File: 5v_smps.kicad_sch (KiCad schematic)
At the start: 1 part

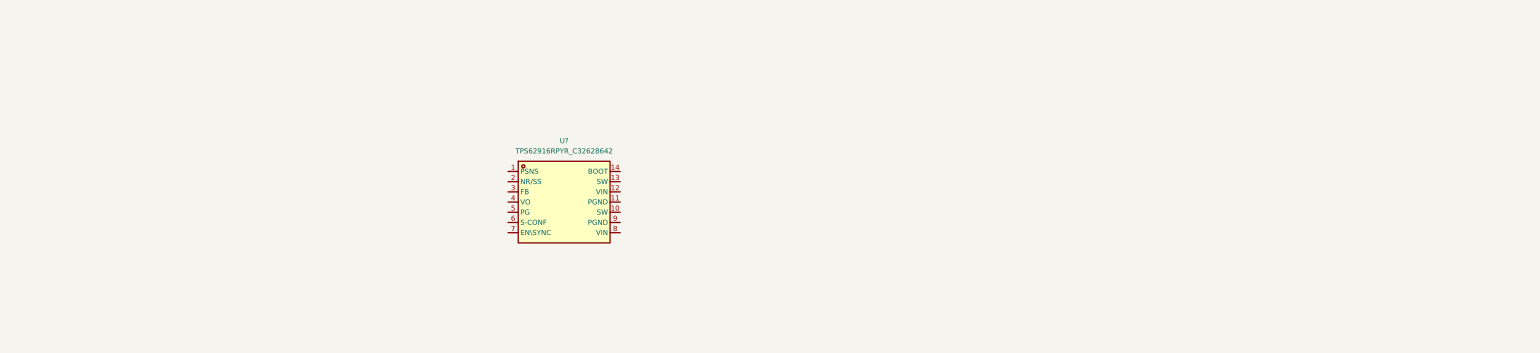
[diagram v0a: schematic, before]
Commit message: updated smps
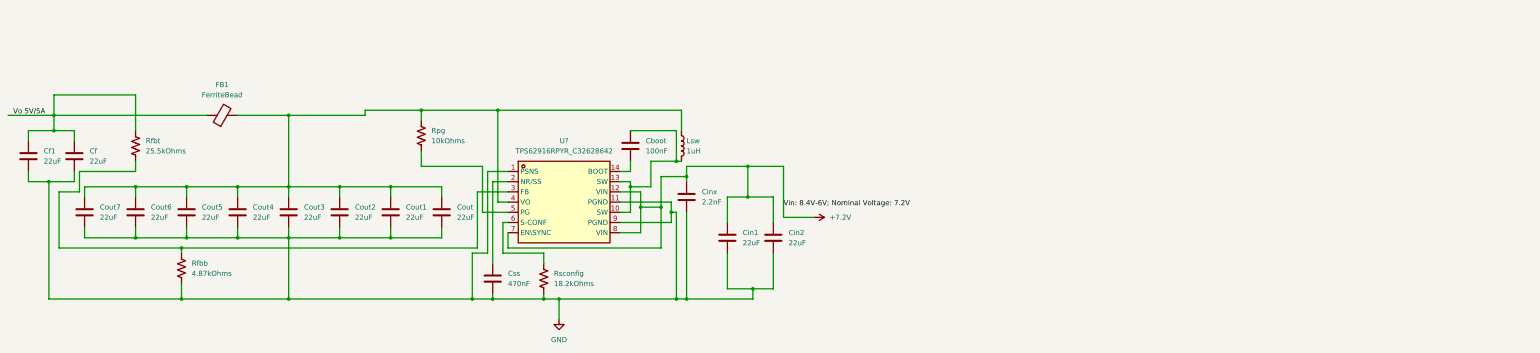
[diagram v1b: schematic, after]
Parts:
- added Cboot: 100nF, symbol Device:C
- added Cf, Cf1, Cin1, Cin2, Cout, Cout1, Cout2, Cout3, Cout4, Cout5, Cout6, Cout7: 22uF, symbol Device:C
- added Cinx: 2.2nF, symbol Device:C
- added Css: 470nF, symbol Device:C
- added FB1: FerriteBead, symbol Device:FerriteBead
- added Lsw: 1uH, symbol Device:L
- added Rfbb: 4.87kOhms, symbol 1_ECE_2300L_Components:Resistor
- added Rfbt: 25.5kOhms, symbol 1_ECE_2300L_Components:Resistor
- added Rpg: 10kOhms, symbol 1_ECE_2300L_Components:Resistor
- added Rsconfig: 18.2kOhms, symbol 1_ECE_2300L_Components:Resistor
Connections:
- net GND: now reaches U?.1 (PSNS)
- net GND: now also U?.11 (PGND), U?.9 (PGND), Cf.2, Cf1.2, Cin1.2, Cin2.2, Cinx.2, Cout.2, Cout1.2, Cout2.2, Cout3.2, Cout4.2, Cout5.2, Cout6.2, Cout7.2, Css.2, Rfbb.2, Rsconfig.2
- net at U?.10 (SW): now also U?.13 (SW), Cboot.1, Lsw.2
- net +7.2V: now reaches U?.12 (VIN)
- net +7.2V: now also U?.7 (EN\SYNC), U?.8 (VIN), Cin1.1, Cin2.1, Cinx.1
- net at U?.14 (BOOT): now also Cboot.2
- net at U?.2 (NR/SS): now also Css.1
- net at U?.3 (FB): now also Rfbb.1, Rfbt.2
- net at U?.4 (VO): now also Cout.1, Cout1.1, Cout2.1, Cout3.1, Cout4.1, Cout5.1, Cout6.1, Cout7.1, FB1.2, Lsw.1, Rpg.1
- net at U?.5 (PG): now also Rpg.2
- net at U?.6 (S-CONF): now also Rsconfig.1
- new net Vo 5V/5A: Cf.1, Cf1.1, FB1.1, Rfbt.1

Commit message: Clean up SMPS schematic
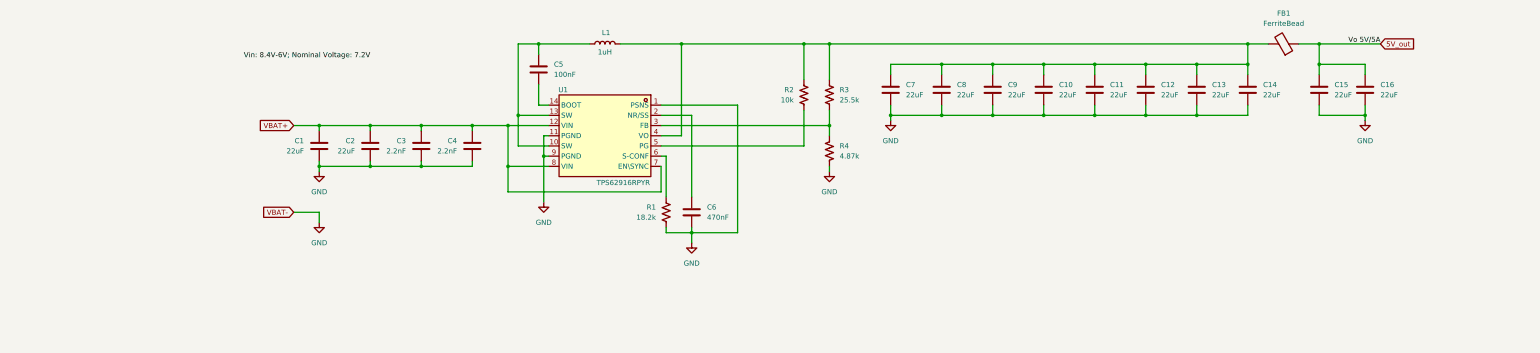
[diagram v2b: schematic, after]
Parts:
- removed Cout1, Cout2, Cout3, Cout4, Cout5, Cout6, Cout7: 22uF, symbol Device:C
- added C10, C11, C12, C13, C14, C8, C9: 22uF, symbol Device:C
- added C4: 2.2nF, Capacitor_SMD:C_0402_1005Metric, symbol Device:C
- C1: renamed from Cin2; footprint (none) -> Capacitor_SMD:C_1210_3225Metric
- C2: renamed from Cin1; footprint (none) -> Capacitor_SMD:C_1210_3225Metric
- C3: renamed from Cinx; footprint (none) -> Capacitor_SMD:C_0402_1005Metric
- R1: renamed from Rsconfig; value 18.2kOhms -> 18.2k
- R2: renamed from Rpg; value 10kOhms -> 10k
- R3: renamed from Rfbt; value 25.5kOhms -> 25.5k
- R4: renamed from Rfbb; value 4.87kOhms -> 4.87k
- U1: renamed from U?; value TPS62916RPYR_C32628642 -> TPS62916RPYR
- renumbered Cf to C15, Cf1 to C16, Cboot to C5, Css to C6, Cout to C7, Lsw to L1
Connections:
- net GND: now also C10.2, C11.2, C12.2, C13.2, C14.2, C4.2, C8.2, C9.2
- net at C7.1, FB1.2, L1.1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: now also R3.1, C10.1, C11.1, C12.1, C13.1, C14.1, C8.1, C9.1
- net +7.2V renamed VBAT+
- net VBAT+: now also C4.1
- net Vo 5V/5A renamed 5V_out
- net 5V_out: no longer R3.1
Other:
- moved on the sheet: C1, C15, C16, C2, C3, C5, C6, C7, FB1, L1, R1, R2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

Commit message: Update 5v_smps.kicad_sch
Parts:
- C10, C11, C12, C13, C14, C15, C16, C5, C7, C8, C9: footprint (none) -> Capacitor_SMD:C_1206_3216Metric
- C3, C4: footprint Capacitor_SMD:C_0402_1005Metric -> Capacitor_SMD:C_0603_1608Metric
- Ce: renamed from C6; footprint (none) -> Capacitor_SMD:C_0603_1608Metric
- FB1: footprint (none) -> 1210
- L1: footprint (none) -> Inductor_SMD:L_Coilcraft_XAL5030-XXX
- R1, R2, R3, R4: footprint (none) -> Resistor_SMD:R_0402_1005Metric
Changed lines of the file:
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@@
 	)
 	(junction
-		(at 271.78 64.77)
+		(at 278.13 59.69)
 		(diameter 0)
 		(color 0 0 0 0)
 	)
 	(junction
-		(at 259.08 77.47)
+		(at 271.78 64.77)
 		(diameter 0)
 		(color 0 0 0 0)
 	)
 	(junction
-		(at 146.05 59.69)
+		(at 259.08 77.47)
 		(diameter 0)
 		(color 0 0 0 0)
 	)
 	(junction
-		(at 322.58 64.77)
+		(at 146.05 59.69)
 		(diameter 0)
 		(color 0 0 0 0)
@@
 	)
 	(junction
-		(at 284.48 77.47)
+		(at 278.13 64.77)
 		(diameter 0)
 		(color 0 0 0 0)
 	)
 	(junction
-		(at 322.58 59.69)
+		(at 284.48 77.47)
 		(diameter 0)
 		(color 0 0 0 0)
@@
 	(wire
 		(pts
-			(xy 322.58 59.69) (xy 322.58 64.77)
+			(xy 176.53 74.93) (xy 195.58 74.93)
 		)
 		(stroke
@@
 	(wire
 		(pts
-			(xy 176.53 74.93) (xy 195.58 74.93)
+			(xy 284.48 67.31) (xy 284.48 64.77)
 		)
 		(stroke
@@
 	(wire
 		(pts
-			(xy 284.48 67.31) (xy 284.48 64.77)
+			(xy 184.15 105.41) (xy 184.15 106.68)
 		)
 		(stroke
@@
 	(wire
 		(pts
-			(xy 184.15 105.41) (xy 184.15 106.68)
+			(xy 278.13 64.77) (xy 284.48 64.77)
 		)
 		(stroke
@@
 	(wire
 		(pts
-			(xy 218.44 59.69) (xy 322.58 59.69)
+			(xy 218.44 59.69) (xy 278.13 59.69)
 		)
 		(stroke
@@
 	(wire
 		(pts
-			(xy 322.58 64.77) (xy 309.88 64.77)
-		)
-		(stroke
-			(width 0)
-			(type default)
-		)
-	)
-	(wire
-		(pts
 			(xy 271.78 77.47) (xy 259.08 77.47)
 		)
@@
 	(wire
 		(pts
+			(xy 233.68 64.77) (xy 233.68 67.31)
+		)
+		(stroke
+			(width 0)
+			(type default)
+		)
+	)
+	(wire
+		(pts
+			(xy 246.38 64.77) (xy 233.68 64.77)
+		)
+		(stroke
+			(width 0)
+			(type default)
+		)
+	)
+	(wire
+		(pts
 			(xy 129.54 80.01) (xy 138.43 80.01)
 		)
@@
 	(wire
 		(pts
+			(xy 278.13 59.69) (xy 278.13 64.77)
+		)
+		(stroke
+			(width 0)
+			(type default)
+		)
+	)
+	(wire
+		(pts
 			(xy 138.43 80.01) (xy 138.43 90.17)
 		)
@@
 	(wire
 		(pts
-			(xy 184.15 106.68) (xy 195.58 106.68)
+			(xy 246.38 64.77) (xy 259.08 64.77)
 		)
 		(stroke
@@
 	(wire
 		(pts
-			(xy 176.53 96.52) (xy 138.43 96.52)
+			(xy 184.15 106.68) (xy 195.58 106.68)
 		)
 		(stroke
@@
 	(wire
 		(pts
-			(xy 233.68 64.77) (xy 246.38 64.77)
+			(xy 176.53 96.52) (xy 138.43 96.52)
 		)
 		(stroke
@@
 	(wire
 		(pts
-			(xy 271.78 64.77) (xy 259.08 64.77)
+			(xy 176.53 82.55) (xy 181.61 82.55)
 		)
 		(stroke
@@
 	(wire
 		(pts
-			(xy 176.53 82.55) (xy 181.61 82.55)
+			(xy 271.78 64.77) (xy 259.08 64.77)
 		)
 		(stroke
@@
 	(wire
 		(pts
-			(xy 284.48 64.77) (xy 271.78 64.77)
+			(xy 309.88 64.77) (xy 297.18 64.77)
 		)
 		(stroke
@@
 	(wire
 		(pts
-			(xy 309.88 64.77) (xy 297.18 64.77)
+			(xy 176.53 85.09) (xy 212.09 85.09)
 		)
 		(stroke
@@
 	(wire
 		(pts
-			(xy 176.53 85.09) (xy 212.09 85.09)
+			(xy 309.88 64.77) (xy 322.58 64.77)
 		)
 		(stroke
@@
 	(wire
 		(pts
-			(xy 177.8 87.63) (xy 177.8 97.79)
+			(xy 284.48 64.77) (xy 297.18 64.77)
 		)
 		(stroke
@@
 	(wire
 		(pts
-			(xy 233.68 67.31) (xy 233.68 64.77)
+			(xy 177.8 87.63) (xy 177.8 97.79)
 		)
 		(stroke
@@
 	(wire
 		(pts
-			(xy 166.37 59.69) (xy 181.61 59.69)
+			(xy 278.13 59.69) (xy 327.66 59.69)
 		)
 		(stroke
@@
 	(wire
 		(pts
-			(xy 271.78 77.47) (xy 271.78 74.93)
+			(xy 166.37 59.69) (xy 181.61 59.69)
 		)
 		(stroke
@@
 	(wire
 		(pts
-			(xy 259.08 64.77) (xy 246.38 64.77)
+			(xy 271.78 77.47) (xy 271.78 74.93)
 		)
 		(stroke
@@
 	(wire
 		(pts
-			(xy 148.59 82.55) (xy 147.32 82.55)
+			(xy 278.13 64.77) (xy 271.78 64.77)
 		)
 		(stroke
@@
 	(wire
 		(pts
-			(xy 322.58 59.69) (xy 327.66 59.69)
+			(xy 148.59 82.55) (xy 147.32 82.55)
 		)
 		(stroke
@@
 	(wire
 		(pts
-			(xy 297.18 64.77) (xy 284.48 64.77)
-		)
-		(stroke
-			(width 0)
-			(type default)
-		)
-	)
-	(wire
-		(pts
 			(xy 116.84 90.17) (xy 129.54 90.17)
 		)
@@
 	)
 	(label "Vin: 8.4V-6V; Nominal Voltage: 7.2V"
-		(at 104.14 63.5 180)
+		(at 86.36 76.2 180)
 		(effects
 			(font
@@
 			)
 		)
-		(property "Footprint" ""
+		(property "Footprint" "Resistor_SMD:R_0402_1005Metric"
 			(at 178.816 101.854 90)
 			(effects
@@
 			)
 		)
-		(property "Footprint" "Capacitor_SMD:C_0402_1005Metric"
+		(property "Footprint" "Capacitor_SMD:C_0603_1608Metric"
 			(at 128.5748 88.9 0)
 			(effects
@@
 			)
 		)
-		(property "Footprint" ""
+		(property "Footprint" "Resistor_SMD:R_0402_1005Metric"
 			(at 219.456 72.644 90)
 			(effects
@@
 			)
 		)
-		(property "Footprint" ""
+		(property "Footprint" "Capacitor_SMD:C_1206_3216Metric"
 			(at 308.9148 74.93 0)
 			(effects
@@
 		(dnp no)
 		(fields_autoplaced yes)
-		(property "Reference" "C6"
+		(property "Reference" "Ce"
 			(at 187.96 100.3299 0)
 			(effects
@@
 			)
 		)
-		(property "Footprint" ""
+		(property "Footprint" "Capacitor_SMD:C_0603_1608Metric"
 			(at 183.1848 105.41 0)
 			(effects
@@
 			(project "ANTS-Power-board"
 				(path "/4d632659-7d2f-4407-ada5-b4e72f7be845/fb60ecbe-8c4e-46ea-aae5-ba0f80fe91e4"
-					(reference "C6")
+					(reference "Ce")
 					(unit 1)
 				)
@@
 			)
 		)
-		(property "Footprint" ""
+		(property "Footprint" "1210"
 			(at 331.47 61.468 90)
 			(effects
@@
 			)
 		)
-		(property "Footprint" ""
+		(property "Footprint" "Resistor_SMD:R_0402_1005Metric"
 			(at 217.424 86.614 90)
 			(effects
@@
 			)
 		)
-		(property "Footprint" ""
+		(property "Footprint" "Capacitor_SMD:C_1206_3216Metric"
 			(at 145.0848 69.85 0)
 			(effects
@@
 			)
 		)
-		(property "Footprint" ""
+		(property "Footprint" "Capacitor_SMD:C_1206_3216Metric"
 			(at 245.4148 74.93 0)
 			(effects
@@
 			)
 		)
-		(property "Footprint" ""
+		(property "Footprint" "Resistor_SMD:R_0402_1005Metric"
 			(at 213.106 72.644 90)
 			(effects
@@
 			)
 		)
-		(property "Footprint" ""
+		(property "Footprint" "Inductor_SMD:L_Coilcraft_XAL5030-XXX"
 			(at 162.56 59.69 0)
 			(effects
@@
 			)
 		)
-		(property "Footprint" ""
+		(property "Footprint" "Capacitor_SMD:C_1206_3216Metric"
 			(at 321.6148 74.93 0)
 			(effects
@@
 			)
 		)
-		(property "Footprint" ""
+		(property "Footprint" "Capacitor_SMD:C_1206_3216Metric"
 			(at 258.1148 74.93 0)
 			(effects
@@
 			)
 		)
-		(property "Footprint" ""
+		(property "Footprint" "Capacitor_SMD:C_1206_3216Metric"
 			(at 270.8148 74.93 0)
 			(effects
@@
 			)
 		)
-		(property "Footprint" "Capacitor_SMD:C_0402_1005Metric"
+		(property "Footprint" "Capacitor_SMD:C_0603_1608Metric"
 			(at 115.8748 88.9 0)
 			(effects
@@
 			)
 		)
-		(property "Footprint" ""
+		(property "Footprint" "Capacitor_SMD:C_1206_3216Metric"
 			(at 283.5148 74.93 0)
 			(effects
@@
 			)
 		)
-		(property "Footprint" ""
+		(property "Footprint" "Capacitor_SMD:C_1206_3216Metric"
 			(at 232.7148 74.93 0)
 			(effects
@@
 			)
 		)
-		(property "Footprint" ""
+		(property "Footprint" "Capacitor_SMD:C_1206_3216Metric"
 			(at 296.2148 74.93 0)
 			(effects
@@
 			)
 		)
-		(property "Footprint" ""
+		(property "Footprint" "Capacitor_SMD:C_1206_3216Metric"
 			(at 350.8248 74.93 0)
 			(effects
@@
 			)
 		)
-		(property "Footprint" ""
+		(property "Footprint" "Capacitor_SMD:C_1206_3216Metric"
 			(at 339.3948 74.93 0)
 			(effects

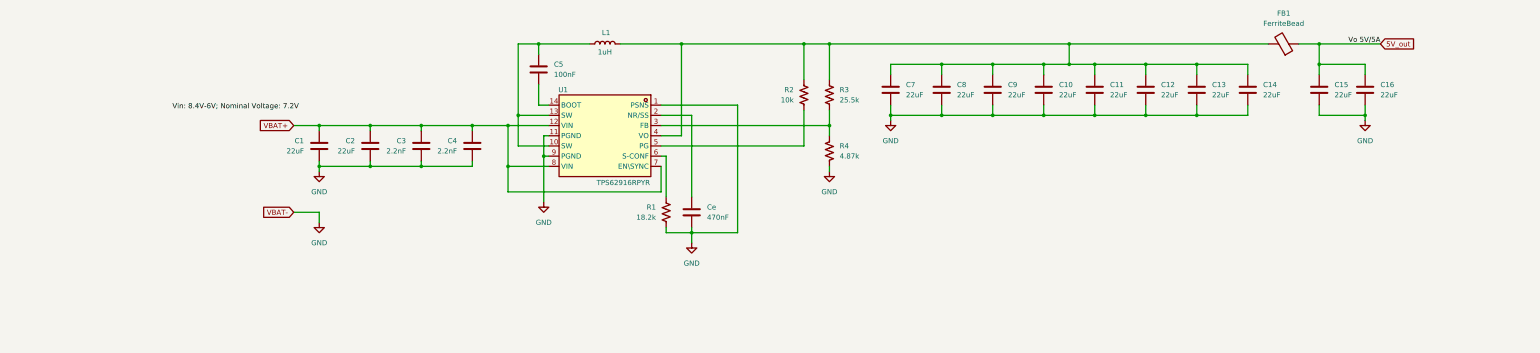
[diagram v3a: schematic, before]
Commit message: Schematic finished; PCB ready for basic layout
Finished the ferrite bead footprint and setup the schematic for the PCB. Schematic has been portered over to the PCB Editor and is ready to start the basic parts layout. The PCB board is set up for the most part there are still some things to set up, but that's for later.
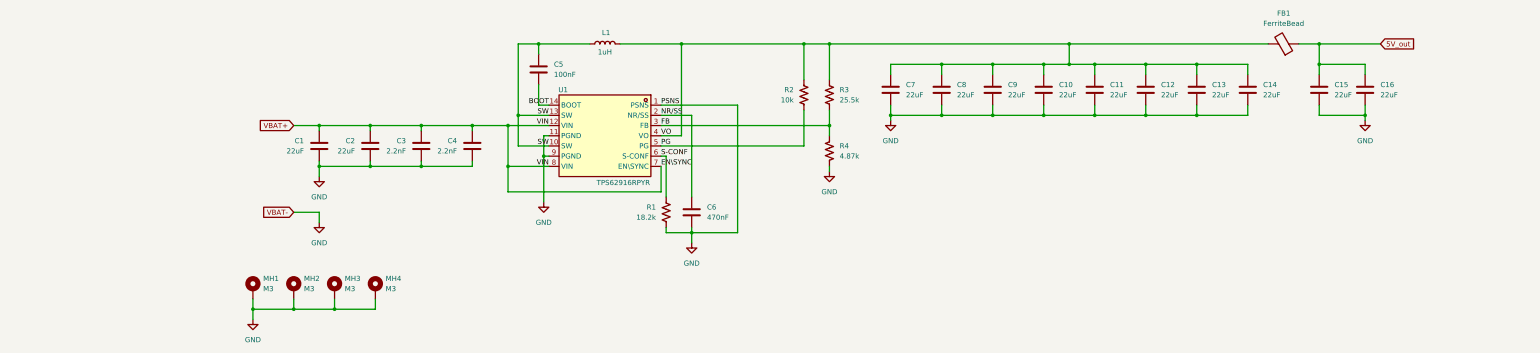
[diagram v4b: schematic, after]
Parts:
- added MH1, MH2, MH3, MH4: M3, MountingHole:MountingHole_3.2mm_M3_Pad_Via, symbol Mechanical:MountingHole_Pad
- FB1: footprint 1210 -> Inductor_SMD:L_1210_3225Metric
- renumbered Ce to C6
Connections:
- net GND: now also MH1.1, MH2.1, MH3.1, MH4.1
- net S-CONF: now reaches R1.1, U1.6 (S-CONF)
- net VO: now reaches C10.1, C11.1, C12.1, C13.1, C14.1, C7.1, C8.1, C9.1, FB1.2, L1.1, R2.1, R3.1, U1.4 (VO)
- net FB: now reaches R3.2, R4.1, U1.3 (FB)
- net NR/SS: now reaches C6.1, U1.2 (NR/SS)
- net SW: now reaches C5.1, L1.2, U1.10 (SW), U1.13 (SW)
- net BOOT: now reaches C5.2, U1.14 (BOOT)
- net PG: now reaches R2.2, U1.5 (PG)

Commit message: Wiring done; grounding and error checking still needs to be done
Wiring done; everything still needs to be grounded, error checking, labeling on the board, and final stuff like that still need to be done
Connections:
- net VO is gone; now on net 5V_out: C10.1, C11.1, C12.1, C13.1, C14.1, C7.1, C8.1, C9.1, FB1.2, L1.1, R2.1, R3.1, U1.4 (VO)
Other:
- moved on the sheet: C15, C16, R3, R4

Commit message: add connections
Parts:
- removed MH1, MH2, MH3, MH4: M3, MountingHole:MountingHole_3.2mm_M3_Pad_Via, symbol Mechanical:MountingHole_Pad
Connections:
- net 5V_out: no longer C10.1, C11.1, C12.1, C13.1, C14.1, C7.1, C8.1, C9.1, FB1.2, L1.1, R2.1, U1.4 (VO)
- new net VO: C10.1, C11.1, C12.1, C13.1, C14.1, C7.1, C8.1, C9.1, FB1.2, L1.1, R2.1, U1.4 (VO)

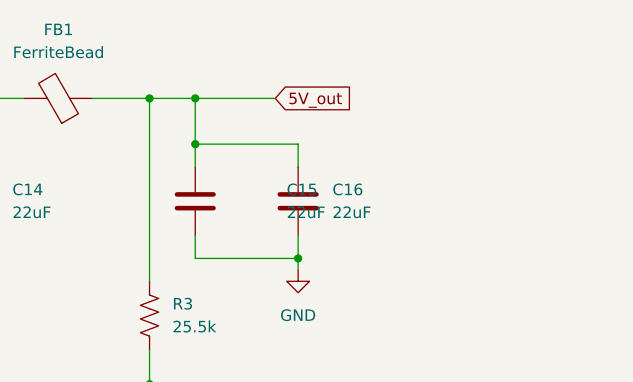
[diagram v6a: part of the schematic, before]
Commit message: Add connectors & adjust board cuts
- Add DF11 and ScrewTerminals
- Add new edge cuts
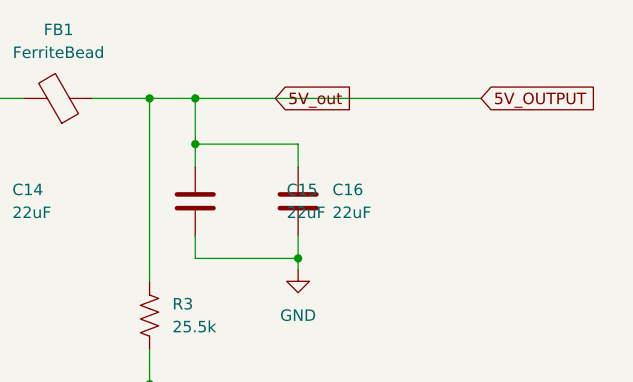
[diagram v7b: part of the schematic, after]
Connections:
- net 5V_out renamed 5V_OUTPUT
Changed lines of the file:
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@@
 	(wire
 		(pts
-			(xy 346.71 59.69) (xy 355.6 59.69)
+			(xy 346.71 59.69) (xy 378.46 59.69)
 		)
 		(stroke
@@
 				(hide yes)
 			)
+		)
+	)
+	(global_label "5V_OUTPUT"
+		(shape input)
+		(at 378.46 59.69 0)
+		(fields_autoplaced yes)
+		(effects
+			(font
+				(size 1.27 1.27)
+			)
+			(justify left)
+		)
+		(property "Intersheetrefs" "${INTERSHEET_REFS}"
+			(at 391.9076 59.69 0)
+			(effects
+				(font
+					(size 1.27 1.27)
+				)
+				(justify left)
+				(hide yes)
+			)
